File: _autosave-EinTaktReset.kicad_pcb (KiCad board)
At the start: 2 copper layers, 35 parts, among them P1 CONN_02X10, P10 CONN_01X01, P11 CONN_01X01, P12 CONN_01X01, P13 CONN_01X01, P14 CONN_01X01, P15 CONN_01X01, P2 CONN_01X01, P3 CONN_01X01, P4 CONN_02X10, P5 CONN_01X01, P6 CONN_01X01, P7 CONN_01X01, P8 CONN_01X01, P9 CONN_01X01, U2 74540En, U3 74HCT541_PWR

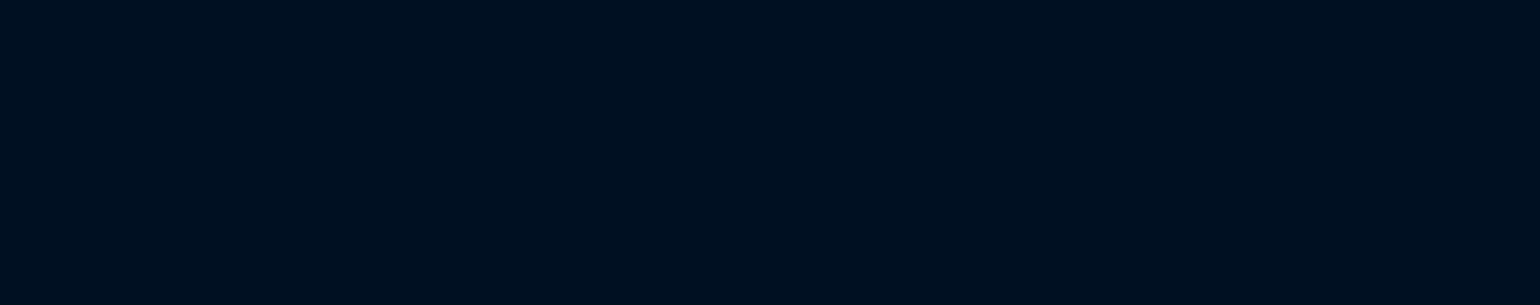
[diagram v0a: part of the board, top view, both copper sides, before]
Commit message: foodprinting EintaktReset2
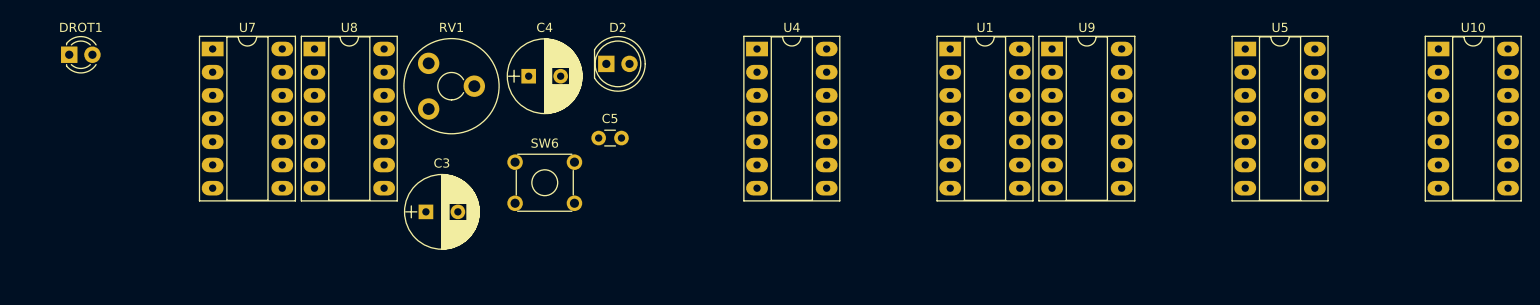
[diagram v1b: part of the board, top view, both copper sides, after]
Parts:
- added C3: 220 µ, Capacitors_ThroughHole:CP_Radial_D8.0mm_P3.50mm, F.Cu at (272.4, 21.1)
- added C4: 220µ, Capacitors_ThroughHole:CP_Radial_D8.0mm_P3.50mm, F.Cu at (283.7, 6.27)
- added C5: 10n, Capacitors_ThroughHole:C_Disc_D3.0mm_W1.6mm_P2.50mm, F.Cu at (291.4, 13.0)
- added D2: LED, LEDs:LED_D5.0mm, F.Cu at (292.2, 4.92)
- added DROT1: LED, LEDs:LED_D3.0mm, F.Cu at (233.4, 3.92)
- added RV1: POT, Potentiometers:Potentiometer_Trimmer_Piher_PT-10v5_Horizontal_Px5.0mm_Py5.0mm, F.Cu at (272.7, 9.86)
- added SW6: SWITCH_INV, Buttons_Switches_ThroughHole:SW_TH_Tactile_Omron_B3F-10xx, F.Cu at (282.2, 15.7)
- added U1: 74LS132, Housings_DIP:DIP-14_W7.62mm_Socket_LongPads, F.Cu at (329.8, 3.29)
- added U10: 74LS00, Housings_DIP:DIP-14_W7.62mm_Socket_LongPads, F.Cu at (383.3, 3.29)
- added U4: 74HCT541_PWR, Housings_DIP:DIP-14_W7.62mm_Socket_LongPads, F.Cu at (308.7, 3.29)
- added U5: 74LS32, Housings_DIP:DIP-14_W7.62mm_Socket_LongPads, F.Cu at (362.1, 3.29)
- added U7: 74LS132, Housings_DIP:DIP-14_W7.62mm_Socket_LongPads, F.Cu at (249.1, 3.29)
- added U8: 74LS32, Housings_DIP:DIP-14_W7.62mm_Socket_LongPads, F.Cu at (260.2, 3.29)
- added U9: 74LS32, Housings_DIP:DIP-14_W7.62mm_Socket_LongPads, F.Cu at (341.0, 3.29)
- U3: value 74HCT541_PWR -> 74LS132
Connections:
- U3 pad 1: Net-(U3-Pad1) -> (no net)
- U3 pad 10: GND -> Net-(U1-Pad11)
- U3 pad 11: /a7 -> (no net)
- U3 pad 12: /a6 -> (no net)
- U3 pad 13: /a5 -> (no net)
- U3 pad 14: /a4 -> VCC
- U3 pad 15: /a3 -> (no net)
- U3 pad 16: /a2 -> (no net)
- U3 pad 17: /a1 -> (no net)
- U3 pad 18: /a0 -> (no net)
- U3 pad 19: Net-(U3-Pad1) -> (no net)
- U3 pad 2: Net-(RP1-Pad2) -> (no net)
- U3 pad 20: VCC -> (no net)
- U3 pad 3: Net-(RP1-Pad3) -> (no net)
- U3 pad 4: Net-(RP1-Pad4) -> (no net)
- U3 pad 5: Net-(RP1-Pad5) -> (no net)
- U3 pad 6: Net-(RP1-Pad6) -> (no net)
- U3 pad 7: Net-(RP1-Pad7) -> GND
- U3 pad 8: Net-(RP1-Pad8) -> Net-(U1-Pad12)
- U3 pad 9: Net-(RP1-Pad9) -> Net-(4,7k1-Pad2)

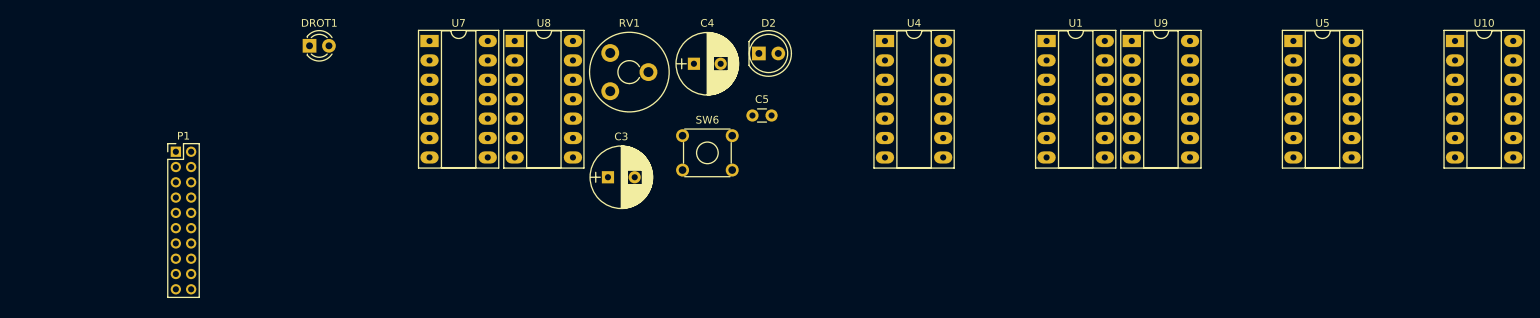
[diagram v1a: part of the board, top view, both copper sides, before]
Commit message: footprint library added
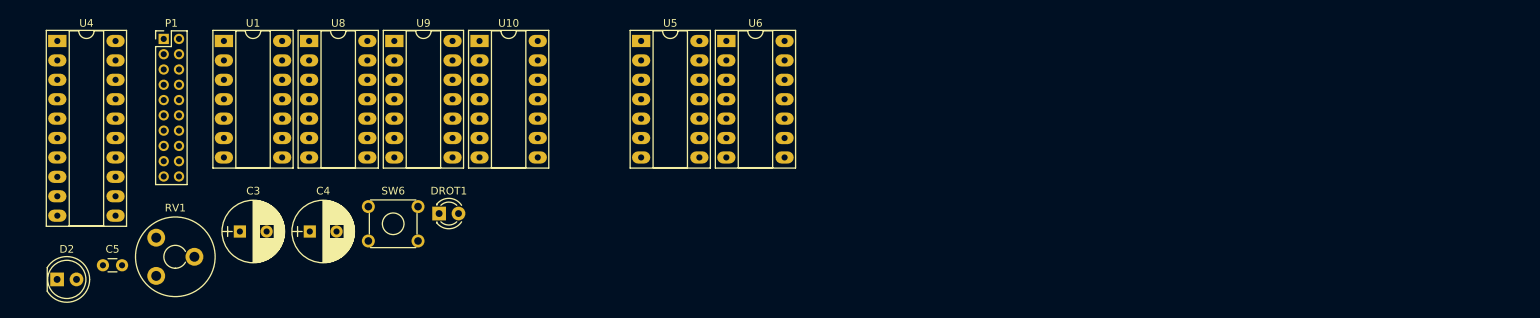
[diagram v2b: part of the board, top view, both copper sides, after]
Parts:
- removed U7: 74LS132, Housings_DIP:DIP-14_W7.62mm_Socket_LongPads
- added U6: 74LS132, Housings_DIP:DIP-14_W7.62mm_Socket_LongPads, F.Cu at (287.9, 3.29)
- U3: value 74LS132 -> 74HCT541_PWR
- U4: value 74HCT541_PWR -> 74LS32; footprint Housings_DIP:DIP-14_W7.62mm_Socket_LongPads -> Housings_DIP:DIP-20_W7.62mm_Socket_LongPads
- U5: value 74LS32 -> 74LS00
- moved U10 127.7 mm to (255.6, 3.29)
- moved U4 108.3 mm to (200.4, 3.29)
- moved U1 107.7 mm to (222.2, 3.29)
- moved U9 96.5 mm to (244.5, 3.29)
- moved D2 96.5 mm to (200.4, 34.5)
- moved C5 87.2 mm to (206.4, 32.6)
- moved U5 85.4 mm to (276.8, 3.29)
- moved RV1 64.1 mm to (213.3, 34.0)
- moved C4 54.9 mm to (233.4, 28.2)
- moved C3 48.7 mm to (224.3, 28.2)
- moved SW6 42.2 mm to (241.1, 25.0)
- moved DROT1 27.7 mm to (250.3, 25.9)
- moved U8 26.9 mm to (233.3, 3.29)
- moved P1 14.8 mm to (214.3, 3.02)
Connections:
- U1 pad 10: (no net) -> Net-(U1-Pad10)
- U1 pad 11: Net-(U1-Pad11) -> Net-(U1-Pad10)
- U1 pad 8: (no net) -> Net-(U1-Pad12)
- U1 pad 9: (no net) -> Net-(4,7k1-Pad2)
- U3 pad 1: (no net) -> Net-(U3-Pad1)
- U3 pad 10: Net-(U1-Pad11) -> GND
- U3 pad 11: (no net) -> /a7
- U3 pad 12: (no net) -> /a6
- U3 pad 13: (no net) -> /a5
- U3 pad 14: VCC -> /a4
- U3 pad 15: (no net) -> /a3
- U3 pad 16: (no net) -> /a2
- U3 pad 17: (no net) -> /a1
- U3 pad 18: (no net) -> /a0
- U3 pad 19: (no net) -> Net-(U3-Pad1)
- U3 pad 2: (no net) -> Net-(RP1-Pad2)
- U3 pad 20: (no net) -> VCC
- U3 pad 3: (no net) -> Net-(RP1-Pad3)
- U3 pad 4: (no net) -> Net-(RP1-Pad4)
- U3 pad 5: (no net) -> Net-(RP1-Pad5)
- U3 pad 6: (no net) -> Net-(RP1-Pad6)
- U3 pad 7: GND -> Net-(RP1-Pad7)
- U3 pad 8: Net-(U1-Pad12) -> Net-(RP1-Pad8)
- U3 pad 9: Net-(4,7k1-Pad2) -> Net-(RP1-Pad9)
- U4 pad 1: Net-(U10-Pad3) -> CLK
- U4 pad 10: GND -> Net-(U1-Pad10)
- U4 pad 11: /a7 -> (no net)
- U4 pad 12: /a6 -> (no net)
- U4 pad 13: /a5 -> (no net)
- U4 pad 14: /a4 -> VCC
- U4 pad 2: Net-(RP1-Pad2) -> CLK
- U4 pad 3: Net-(RP1-Pad3) -> Net-(R4-Pad1)
- U4 pad 4: Net-(RP1-Pad4) -> Net-(U3-Pad1)
- U4 pad 5: Net-(RP1-Pad5) -> Net-(U3-Pad1)
- U4 pad 6: Net-(RP1-Pad6) -> Net-(R7-Pad1)
- U4 pad 7: Net-(RP1-Pad7) -> GND
- U4 pad 8: Net-(RP1-Pad8) -> CLK
- U4 pad 9: Net-(RP1-Pad9) -> Net-(U4-Pad9)
- U5 pad 1: CLK -> Net-(IC1-Pad8)
- U5 pad 10: (no net) -> Net-(U5-Pad10)
- U5 pad 11: (no net) -> Net-(U5-Pad10)
- U5 pad 12: (no net) -> en-ln1
- U5 pad 13: (no net) -> en-ln2
- U5 pad 2: CLK -> Net-(U1-Pad6)
- U5 pad 3: Net-(R4-Pad1) -> Net-(U5-Pad3)
- U5 pad 4: (no net) -> Net-(U5-Pad3)
- U5 pad 5: (no net) -> Net-(U5-Pad3)
- U5 pad 6: (no net) -> Net-(U4-Pad9)
- U5 pad 8: (no net) -> Net-(U3-Pad1)
- U5 pad 9: (no net) -> Net-(U5-Pad10)
